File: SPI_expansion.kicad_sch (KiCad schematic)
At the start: 13 parts, among them J16 Conn_02x05_Odd_Even, J17 Conn_02x03_Odd_Even, J18 Conn_02x03_Odd_Even, J19 Conn_02x03_Odd_Even, J9 Conn_02x05_Odd_Even

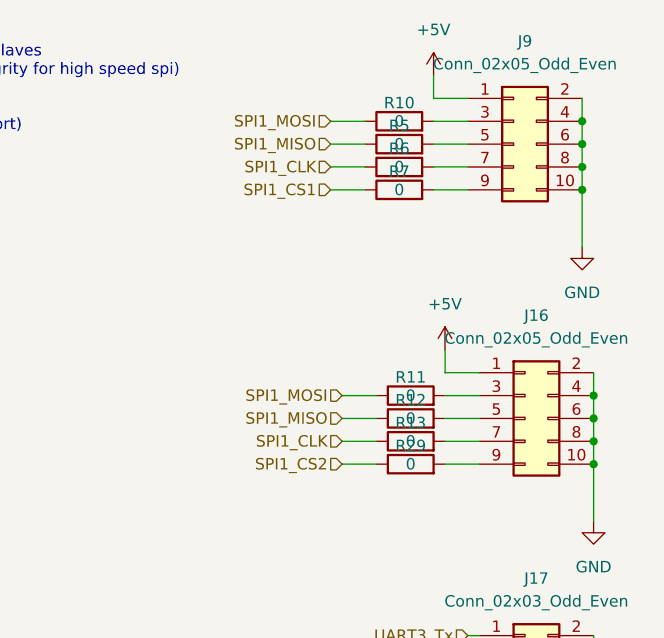
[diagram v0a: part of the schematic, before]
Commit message: Key CHanges for connector choices , termination and semi-final decisions on them
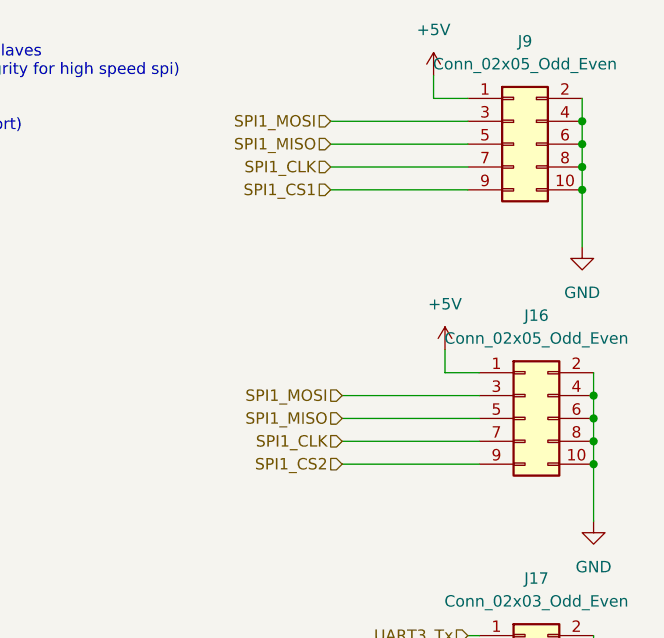
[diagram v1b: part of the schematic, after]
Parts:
- removed R10, R11, R12, R13, R29, R5, R6, R7: 0, Resistor_SMD:R_0805_2012Metric, symbol Device:R
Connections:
- net SPI1_CLK: now also J16.7 (Pin_7), J9.7 (Pin_7)
- net SPI1_CS1: now also J9.9 (Pin_9)
- net SPI1_CS2: now also J16.9 (Pin_9)
- net SPI1_MISO: now also J16.5 (Pin_5), J9.5 (Pin_5)
- net SPI1_MOSI: now also J16.3 (Pin_3), J9.3 (Pin_3)

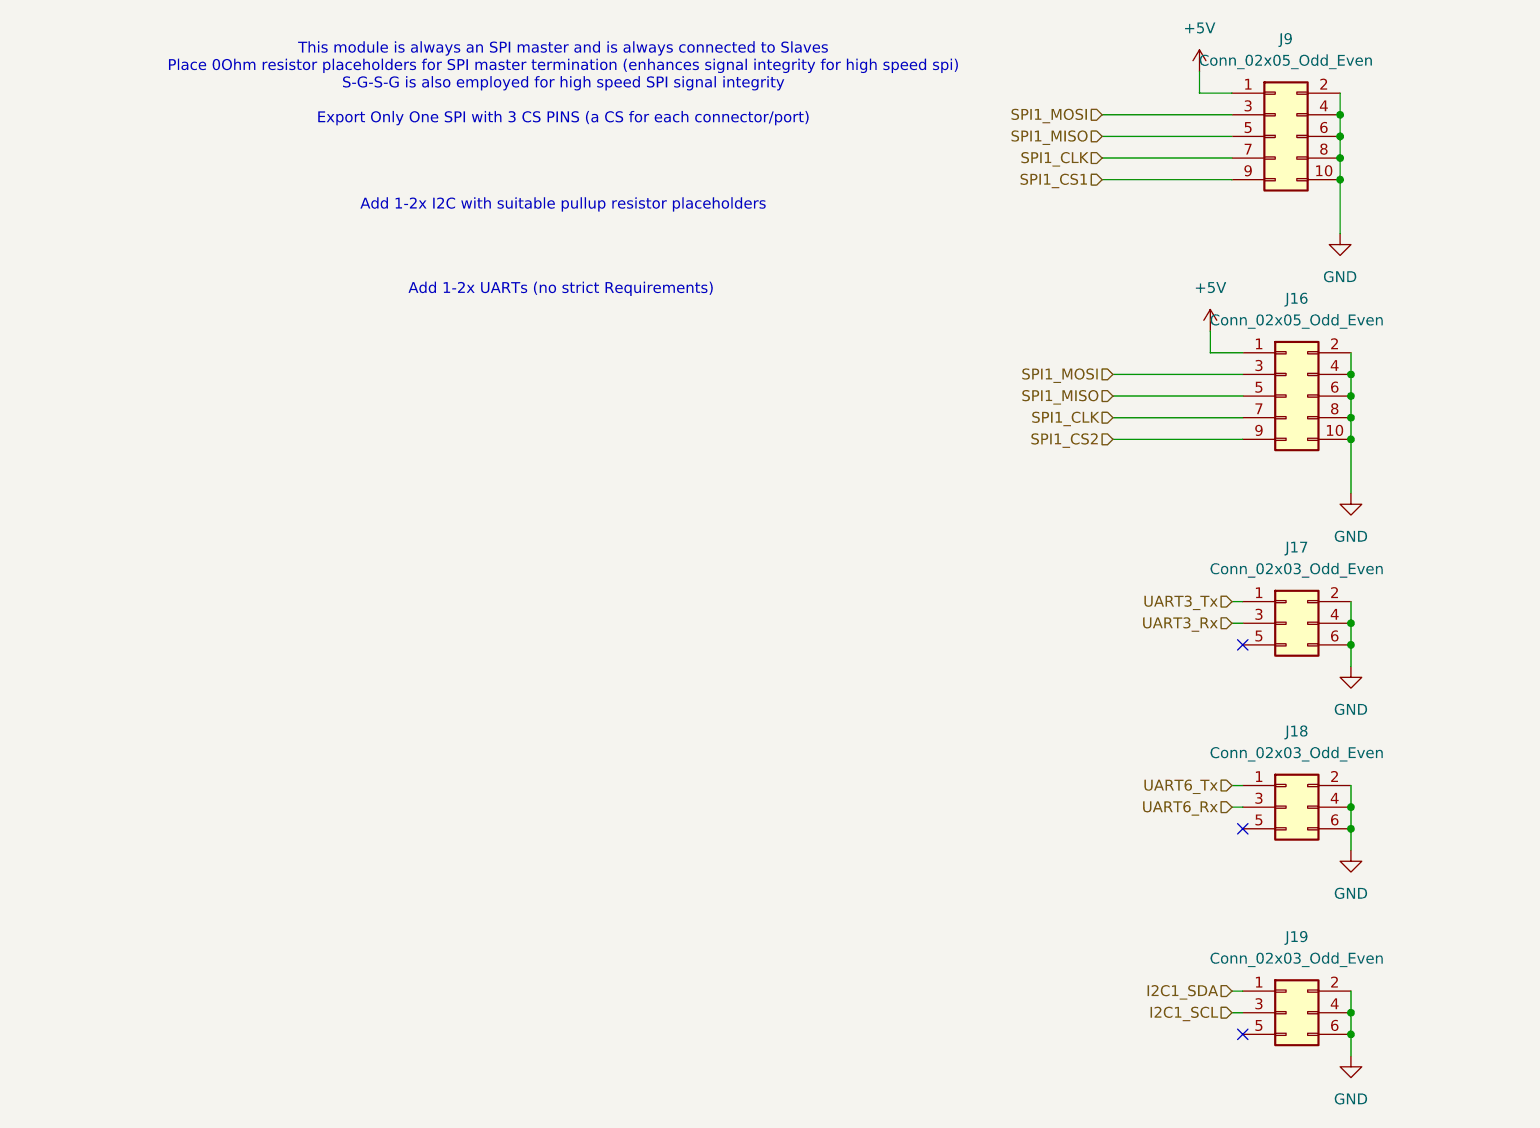
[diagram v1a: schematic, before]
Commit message: Done routing for Buck Converter , Rs485 and CAN , Some Routing for MCU and associated circuitry , NO ETHERNET ROUTING , NO module Interconnects yet
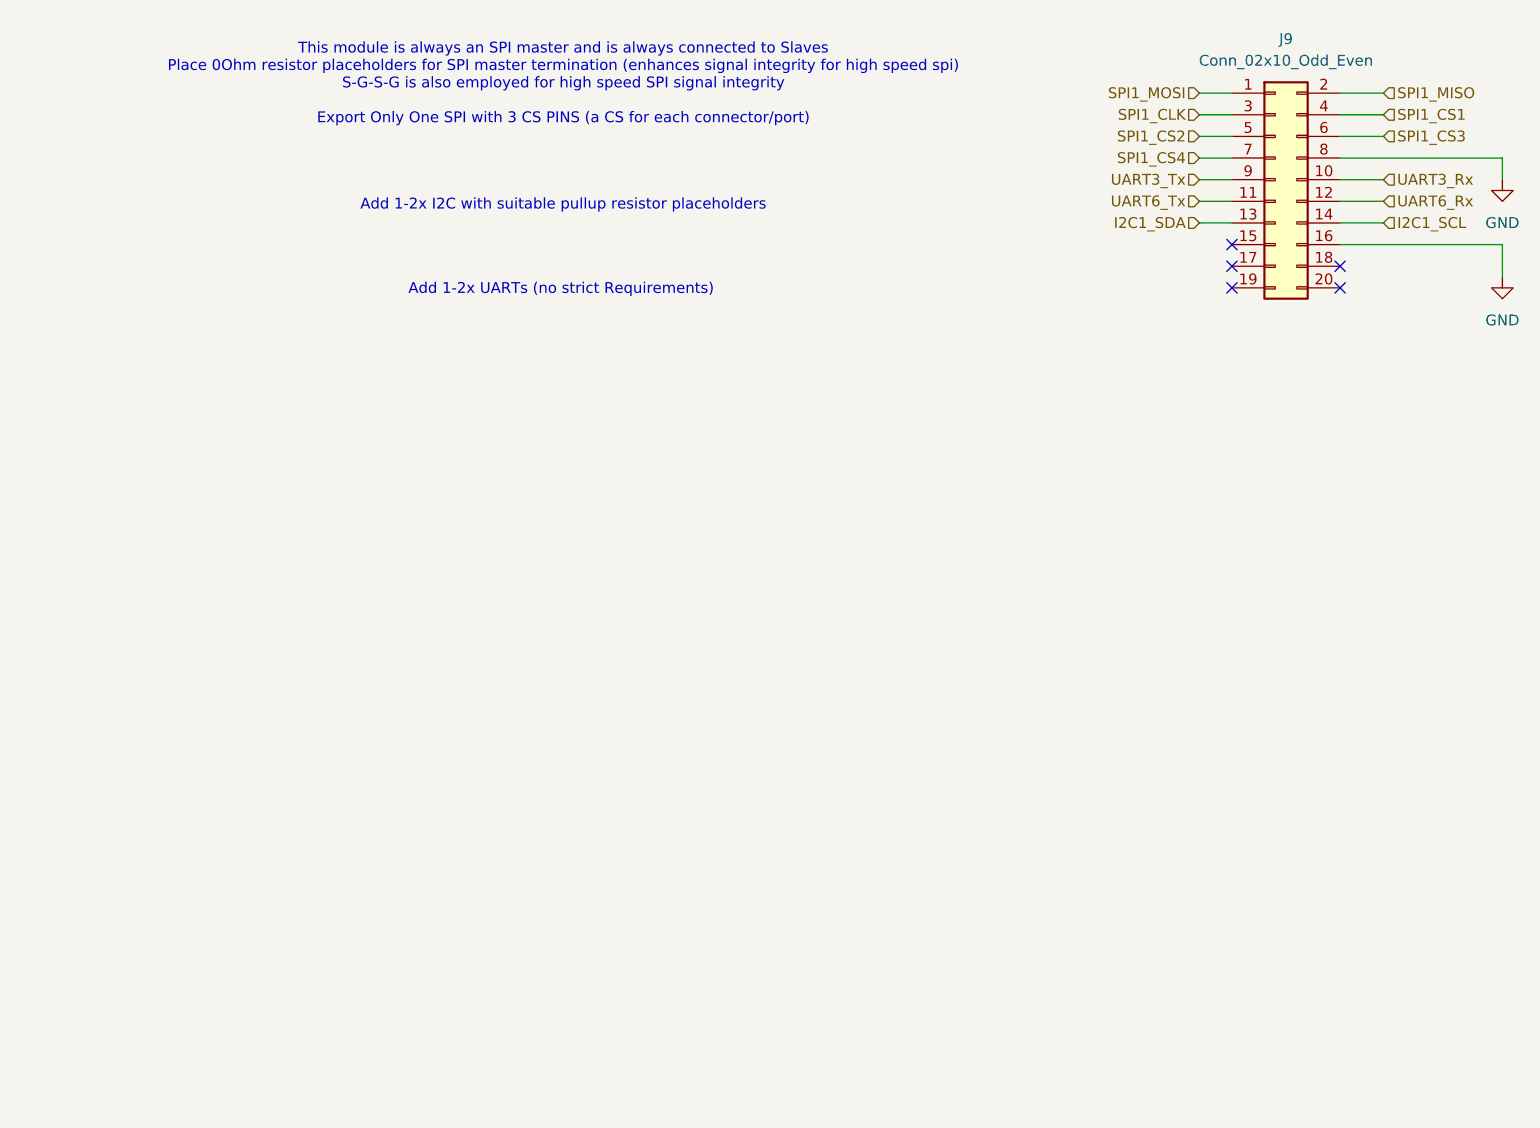
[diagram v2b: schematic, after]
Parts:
- removed J16, J9: Conn_02x05_Odd_Even, Connector_IDC:IDC-Header_2x05_P2.54mm_Vertical, symbol Connector_Generic:Conn_02x05_Odd_Even
- removed J17, J18, J19: Conn_02x03_Odd_Even, Connector_IDC:IDC-Header_2x03_P2.54mm_Vertical, symbol Connector_Generic:Conn_02x03_Odd_Even
- added J9: Conn_02x10_Odd_Even, Connector_IDC:IDC-Header_2x10_P2.54mm_Vertical, symbol Connector_Generic:Conn_02x10_Odd_Even
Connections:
- net GND: now also J9.16 (Pin_16), J9.8 (Pin_8)
- net I2C1_SCL: now also J9.14 (Pin_14)
- net I2C1_SDA: now also J9.13 (Pin_13)
- net SPI1_CLK: now also J9.3 (Pin_3)
- net SPI1_CS1: now also J9.4 (Pin_4)
- net SPI1_CS2: now also J9.5 (Pin_5)
- net SPI1_MISO: now also J9.2 (Pin_2)
- net SPI1_MOSI: now also J9.1 (Pin_1)
- net UART3_Rx: now also J9.10 (Pin_10)
- net UART3_Tx: now also J9.9 (Pin_9)
- net UART6_Rx: now also J9.12 (Pin_12)
- net UART6_Tx: now also J9.11 (Pin_11)
- new net SPI1_CS3: J9.6 (Pin_6)
- new net SPI1_CS4: J9.7 (Pin_7)
- no-connect marks 3 -> 5
